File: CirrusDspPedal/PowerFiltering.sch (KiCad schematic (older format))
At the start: 5 parts

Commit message: updates
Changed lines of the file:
@@
 $Descr A4 11693 8268
 encoding utf-8
-Sheet 3 11
+Sheet 3 10
 Title ""
 Date ""
@@
 AR Path="/5F834C36/5F85DD92/5F85FD42" Ref="C9"  Part="1"
 AR Path="/5F834DC7/5F893E1B/5F85FD42" Ref="C17"  Part="1"
-F 0 "C17" H 6940 3746 50  0000 L CNN
+F 0 "C9" H 6940 3746 50  0000 L CNN
 F 1 "100nF" H 6940 3655 50  0000 L CNN
 F 2 "Capacitor_SMD:C_0805_2012Metric_Pad1.15x1.40mm_HandSolder" H 6863 3550 50  0001 C CNN
@@
 AR Path="/5F834C36/5F85DD92/5F85FD48" Ref="C7"  Part="1"
 AR Path="/5F834DC7/5F893E1B/5F85FD48" Ref="C15"  Part="1"
-F 0 "C15" H 4390 3746 50  0000 L CNN
+F 0 "C7" H 4390 3746 50  0000 L CNN
 F 1 "100nF" H 4390 3655 50  0000 L CNN
 F 2 "Capacitor_SMD:C_0805_2012Metric_Pad1.15x1.40mm_HandSolder" H 4313 3550 50  0001 C CNN
@@
 AR Path="/5F834C36/5F85DD92/5F85FD4E" Ref="C8"  Part="1"
 AR Path="/5F834DC7/5F893E1B/5F85FD4E" Ref="C16"  Part="1"
-F 0 "C16" H 5790 3396 50  0000 L CNN
+F 0 "C8" H 5790 3396 50  0000 L CNN
 F 1 "100nF" H 5790 3305 50  0000 L CNN
 F 2 "Capacitor_SMD:C_0805_2012Metric_Pad1.15x1.40mm_HandSolder" H 5713 3200 50  0001 C CNN
@@
 AR Path="/5F834C36/5F85DD92/5F85FD54" Ref="R4"  Part="1"
 AR Path="/5F834DC7/5F893E1B/5F85FD54" Ref="R7"  Part="1"
-F 0 "R7" H 5745 4146 50  0000 L CNN
+F 0 "R4" H 5745 4146 50  0000 L CNN
 F 1 "1R 1%" H 5745 4055 50  0000 L CNN
 F 2 "Resistor_SMD:R_0805_2012Metric_Pad1.15x1.40mm_HandSolder" V 5605 4100 50  0001 C CNN
@@
 AR Path="/5F834C36/5F85DD92/5F85FD69" Ref="FB1"  Part="1"
 AR Path="/5F834DC7/5F893E1B/5F85FD69" Ref="FB2"  Part="1"
-F 0 "FB2" V 4788 2900 50  0000 C CNN
+F 0 "FB1" V 4788 2900 50  0000 C CNN
 F 1 "600" V 4879 2900 50  0000 C CNN
 F 2 "Inductor_SMD:L_0805_2012Metric_Pad1.15x1.40mm_HandSolder" V 4955 2900 50  0001 C CNN
@@
 AR Path="/5F834C36/5F85DD92/5F85FD73" Ref="#PWR0109"  Part="1"
 AR Path="/5F834DC7/5F893E1B/5F85FD73" Ref="#PWR0116"  Part="1"
-F 0 "#PWR0116" H 3900 4675 50  0001 C CNN
+F 0 "#PWR0109" H 3900 4675 50  0001 C CNN
 F 1 "GNDS" H 3905 4752 50  0000 C CNN
 F 2 "" H 3900 4925 50  0001 C CNN

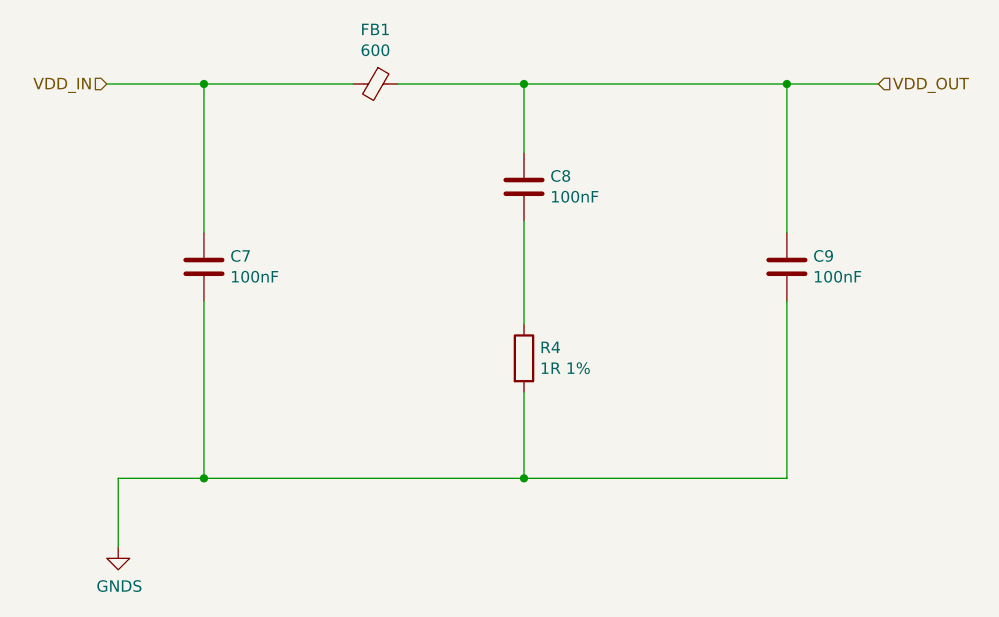
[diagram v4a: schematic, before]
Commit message: updated design and layout
- Changed LDO package from SOT23 to SOT223
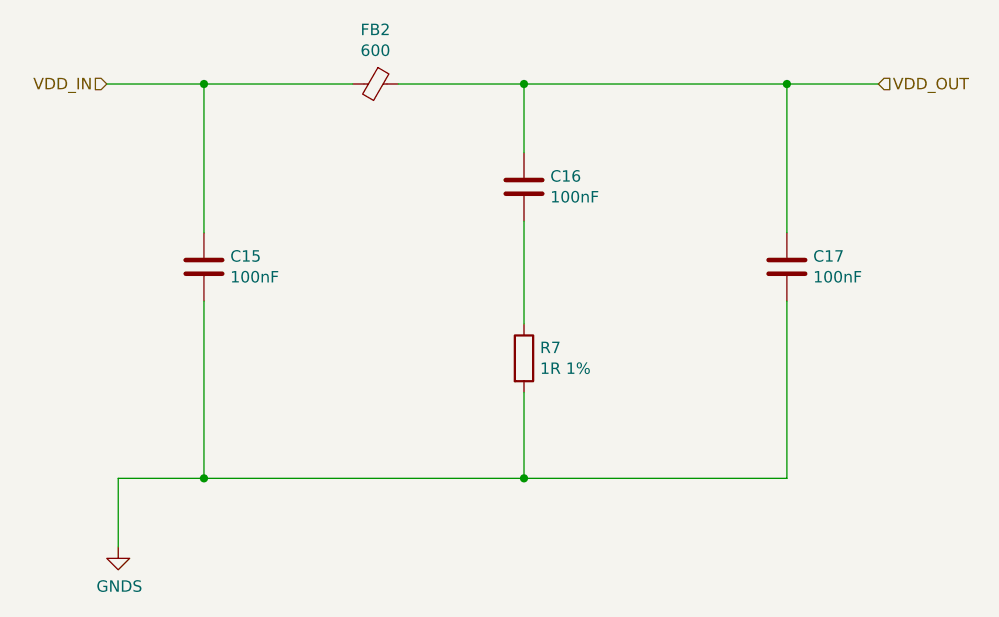
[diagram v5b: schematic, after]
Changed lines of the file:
@@
 $Descr A4 11693 8268
 encoding utf-8
-Sheet 3 10
+Sheet 5 10
 Title ""
 Date ""
@@
 AR Path="/5F834C36/5F85DD92/5F85FD42" Ref="C9"  Part="1"
 AR Path="/5F834DC7/5F893E1B/5F85FD42" Ref="C17"  Part="1"
-F 0 "C9" H 6940 3746 50  0000 L CNN
+F 0 "C17" H 6940 3746 50  0000 L CNN
 F 1 "100nF" H 6940 3655 50  0000 L CNN
 F 2 "Capacitor_SMD:C_0805_2012Metric_Pad1.15x1.40mm_HandSolder" H 6863 3550 50  0001 C CNN
@@
 AR Path="/5F834C36/5F85DD92/5F85FD48" Ref="C7"  Part="1"
 AR Path="/5F834DC7/5F893E1B/5F85FD48" Ref="C15"  Part="1"
-F 0 "C7" H 4390 3746 50  0000 L CNN
+F 0 "C15" H 4390 3746 50  0000 L CNN
 F 1 "100nF" H 4390 3655 50  0000 L CNN
 F 2 "Capacitor_SMD:C_0805_2012Metric_Pad1.15x1.40mm_HandSolder" H 4313 3550 50  0001 C CNN
@@
 AR Path="/5F834C36/5F85DD92/5F85FD4E" Ref="C8"  Part="1"
 AR Path="/5F834DC7/5F893E1B/5F85FD4E" Ref="C16"  Part="1"
-F 0 "C8" H 5790 3396 50  0000 L CNN
+F 0 "C16" H 5790 3396 50  0000 L CNN
 F 1 "100nF" H 5790 3305 50  0000 L CNN
 F 2 "Capacitor_SMD:C_0805_2012Metric_Pad1.15x1.40mm_HandSolder" H 5713 3200 50  0001 C CNN
@@
 AR Path="/5F834C36/5F85DD92/5F85FD54" Ref="R4"  Part="1"
 AR Path="/5F834DC7/5F893E1B/5F85FD54" Ref="R7"  Part="1"
-F 0 "R4" H 5745 4146 50  0000 L CNN
+F 0 "R7" H 5745 4146 50  0000 L CNN
 F 1 "1R 1%" H 5745 4055 50  0000 L CNN
 F 2 "Resistor_SMD:R_0805_2012Metric_Pad1.15x1.40mm_HandSolder" V 5605 4100 50  0001 C CNN
@@
 AR Path="/5F834C36/5F85DD92/5F85FD69" Ref="FB1"  Part="1"
 AR Path="/5F834DC7/5F893E1B/5F85FD69" Ref="FB2"  Part="1"
-F 0 "FB1" V 4788 2900 50  0000 C CNN
+F 0 "FB2" V 4788 2900 50  0000 C CNN
 F 1 "600" V 4879 2900 50  0000 C CNN
 F 2 "Inductor_SMD:L_0805_2012Metric_Pad1.15x1.40mm_HandSolder" V 4955 2900 50  0001 C CNN
